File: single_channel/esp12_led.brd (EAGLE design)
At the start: 100 x 80 mm, 10 parts

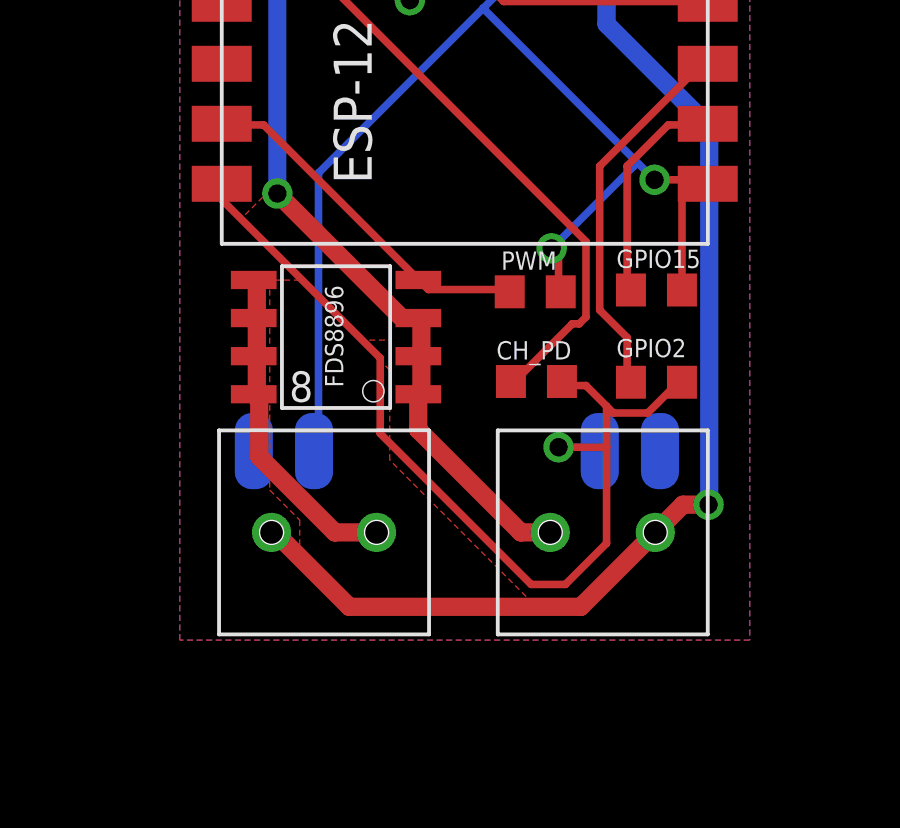
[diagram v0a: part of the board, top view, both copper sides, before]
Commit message: Improved design: Added triple channel (RGB) support, beefed up to ~8.5A per channel.
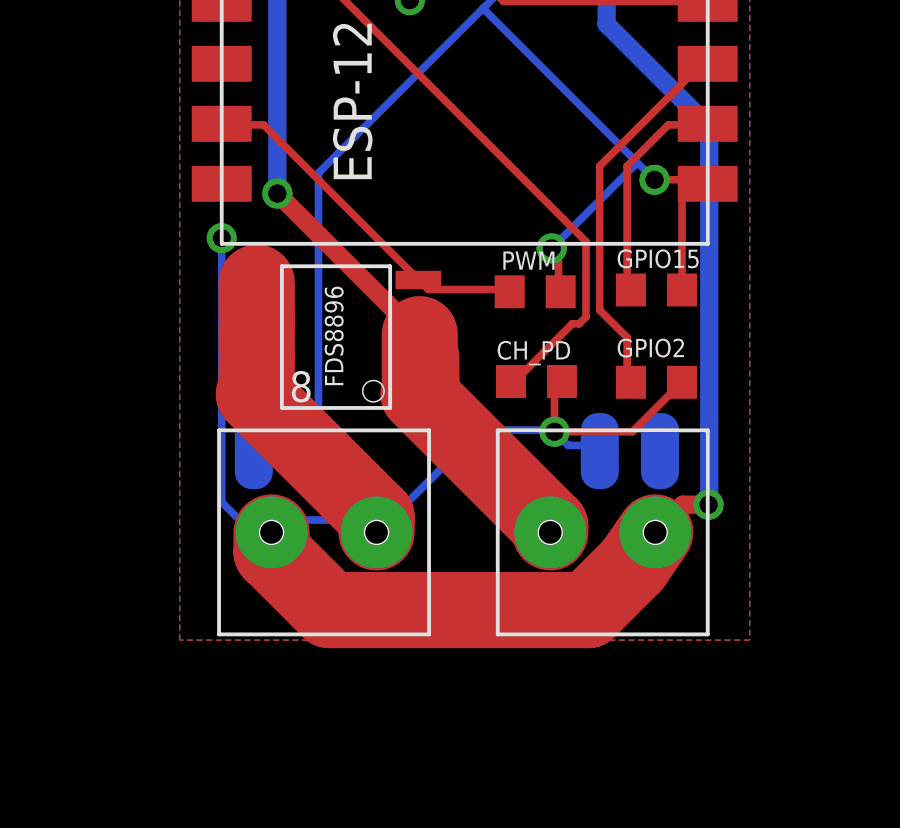
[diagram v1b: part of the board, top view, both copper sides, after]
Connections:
- new net S$3: 12V_IN.1, FDS8896.1, FDS8896.2
- net N$10: no longer 12V_IN.1, FDS8896.1, FDS8896.2
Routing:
- net S$3: track 0.00 -> 10.00 mm
- net N$10: track 26.9 -> 17.4 mm
- net N$1: track 33.2 -> 29.9 mm, vias 1 -> 2
- net N$4: track 11.2 -> 10.4 mm
- net N$12: track 39.4 -> 40.0 mm
- removed copper zone on layer 1, net S$4
- removed copper zone on layer 1, net S$5
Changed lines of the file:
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@@
 <signals>
 <signal name="S$1">
-<polygon width="0.1" layer="1" spacing="0.3048" pour="hatch" isolate="0.254">
+<polygon width="0.1" layer="1" spacing="0.3048" isolate="0.254">
 <vertex x="33" y="53.43"/>
 <vertex x="52" y="53.43"/>
@@
 <vertex x="33" y="23"/>
 </polygon>
-<polygon width="0.1" layer="16" spacing="0.3048" pour="hatch" isolate="0.254">
+<polygon width="0.1" layer="16" spacing="0.3048" isolate="0.254">
 <vertex x="33" y="53.43"/>
 <vertex x="52" y="53.43"/>
@@
 <contactref element="DC_CONVERTER" pad="OUT+(1)"/>
 <contactref element="ESP-12" pad="16"/>
-<wire x1="46.5412" y1="31.4856" x2="45.8554" y2="31.4856" width="0.254" layer="1"/>
-<wire x1="47.4556" y1="30.5712" x2="47.227" y2="30.7998" width="0.254" layer="1"/>
-<wire x1="47.227" y1="30.7998" x2="46.5412" y2="31.4856" width="0.254" layer="1"/>
-<wire x1="48.5986" y1="30.5712" x2="47.4556" y2="30.5712" width="0.254" layer="1"/>
-<wire x1="49.513" y1="31.4856" x2="48.5986" y2="30.5712" width="0.254" layer="1"/>
-<wire x1="45.8554" y1="31.4856" x2="45.74" y2="31.62" width="0.254" layer="1"/>
-<wire x1="49.513" y1="31.4856" x2="49.74" y2="31.595" width="0.254" layer="1"/>
-<wire x1="34.4254" y1="37.6578" x2="34.4254" y2="38.115" width="0.254" layer="1"/>
-<wire x1="39.6832" y1="32.4" x2="34.4254" y2="37.6578" width="0.254" layer="1"/>
-<wire x1="39.6832" y1="29.8854" x2="39.6832" y2="32.4" width="0.254" layer="1"/>
-<wire x1="44.7124" y1="24.8562" x2="39.6832" y2="29.8854" width="0.254" layer="1"/>
-<wire x1="45.8554" y1="24.8562" x2="44.7124" y2="24.8562" width="0.254" layer="1"/>
-<wire x1="47.227" y1="26.2278" x2="45.8554" y2="24.8562" width="0.254" layer="1"/>
-<wire x1="47.227" y1="30.7998" x2="47.227" y2="29.4282" width="0.254" layer="1"/>
-<wire x1="47.227" y1="29.4282" x2="47.227" y2="26.2278" width="0.254" layer="1"/>
-<wire x1="34.4254" y1="38.115" x2="34.4" y2="38.21" width="0.254" layer="1"/>
-<wire x1="45.6268" y1="29.4282" x2="46.9984" y2="29.4282" width="0.254" layer="16"/>
-<wire x1="47.227" y1="29.4282" x2="45.6268" y2="29.4282" width="0.254" layer="1"/>
-<wire x1="46.9984" y1="29.4282" x2="47.0016" y2="29.3" width="0.254" layer="16"/>
-<via x="45.6268" y="29.4282" extent="1-16" drill="0.6096"/>
+<wire x1="45.9486" y1="29.4894" x2="46.863" y2="29.4894" width="0.254" layer="16"/>
+<wire x1="45.4914" y1="29.9466" x2="45.9486" y2="29.4894" width="0.254" layer="16"/>
+<wire x1="45.4914" y1="31.3182" x2="45.4914" y2="29.9466" width="0.254" layer="1"/>
+<wire x1="45.72" y1="31.5468" x2="45.4914" y2="31.3182" width="0.254" layer="1"/>
+<wire x1="46.863" y1="29.4894" x2="47.0016" y2="29.3" width="0.254" layer="16"/>
+<wire x1="45.72" y1="31.5468" x2="45.74" y2="31.62" width="0.254" layer="1"/>
+<via x="45.4914" y="29.9466" extent="1-16" drill="0.6096"/>
+<via x="34.4" y="36.4" extent="1-16" drill="0.6"/>
+<wire x1="34.4" y1="36.4" x2="34.4" y2="27.6" width="0.254" layer="16"/>
+<wire x1="34.4" y1="27.6" x2="35" y2="27" width="0.254" layer="16"/>
+<wire x1="35" y1="27" x2="40" y2="27" width="0.254" layer="16"/>
+<wire x1="40" y1="27" x2="43" y2="30" width="0.254" layer="16"/>
+<wire x1="43" y1="30" x2="45.438" y2="30" width="0.254" layer="16"/>
+<wire x1="45.438" y1="30" x2="45.4914" y2="29.9466" width="0.254" layer="16"/>
+<wire x1="49.74" y1="31.595" x2="48.0916" y2="29.9466" width="0.254" layer="1"/>
+<wire x1="48.0916" y1="29.9466" x2="45.4914" y2="29.9466" width="0.254" layer="1"/>
+<wire x1="34.4" y1="36.4" x2="34.4" y2="38.21" width="0" layer="19" extent="1-1"/>
 </signal>
 <signal name="N$2">
@@
 <contactref element="FDS8896" pad="8"/>
 <contactref element="LED" pad="2"/>
-<wire x1="35.5684" y1="32.4" x2="35.5684" y2="31.257" width="0.6096" layer="1"/>
+<wire x1="35.5684" y1="32.4" x2="35.5684" y2="31.257" width="2.54" layer="1"/>
 <wire x1="35.5684" y1="31.257" x2="35.4668" y2="31.195" width="0.254" layer="1"/>
 <wire x1="35.5684" y1="32.4" x2="35.4668" y2="32.465" width="0.254" layer="1"/>
-<wire x1="35.5684" y1="32.6286" x2="35.5684" y2="33.543" width="0.6096" layer="1"/>
+<wire x1="35.5684" y1="32.6286" x2="35.5684" y2="33.543" width="2.54" layer="1"/>
 <wire x1="35.5684" y1="33.543" x2="35.4668" y2="33.735" width="0.254" layer="1"/>
 <wire x1="35.5684" y1="32.6286" x2="35.4668" y2="32.465" width="0.254" layer="1"/>
-<wire x1="35.5684" y1="33.7716" x2="35.5684" y2="34.9146" width="0.6096" layer="1"/>
+<wire x1="35.5684" y1="33.7716" x2="35.5684" y2="34.9146" width="2.54" layer="1"/>
 <wire x1="35.5684" y1="34.9146" x2="35.4668" y2="35.005" width="0.254" layer="1"/>
 <wire x1="35.5684" y1="33.7716" x2="35.4668" y2="33.735" width="0.254" layer="1"/>
-<wire x1="39.56" y1="26.59" x2="38.17" y2="26.59" width="0.6096" layer="1"/>
-<wire x1="38.17" y1="26.59" x2="35.65" y2="29.11" width="0.6096" layer="1"/>
-<wire x1="35.65" y1="29.11" x2="35.65" y2="31.0118" width="0.6096" layer="1"/>
-<wire x1="35.65" y1="31.0118" x2="35.4668" y2="31.195" width="0.6096" layer="1"/>
+<wire x1="39.56" y1="26.59" x2="39.56" y2="27.1018" width="2.54" layer="1"/>
+<wire x1="39.56" y1="27.1018" x2="35.4668" y2="31.195" width="2.54" layer="1"/>
+</signal>
+<signal name="S$3">
+<contactref element="FDS8896" pad="2"/>
+<wire x1="41.0548" y1="32.6286" x2="40.9532" y2="32.465" width="0.254" layer="1"/>
+<contactref element="FDS8896" pad="1"/>
+<wire x1="41.0548" y1="32.4" x2="40.9532" y2="32.465" width="0.254" layer="1"/>
+<wire x1="41.0548" y1="32.4" x2="41.0548" y2="31.257" width="2.54" layer="1"/>
+<wire x1="41.0548" y1="31.257" x2="40.9532" y2="31.195" width="0.254" layer="1"/>
+<contactref element="12V_IN" pad="1"/>
+<wire x1="41.0548" y1="31.257" x2="41" y2="31.257" width="2.54" layer="1"/>
+<wire x1="41" y1="31.257" x2="41" y2="33.2" width="2.54" layer="1"/>
+<wire x1="45.35" y1="26.59" x2="45.35" y2="26.7982" width="2.54" layer="1"/>
+<wire x1="45.35" y1="26.7982" x2="40.9532" y2="31.195" width="2.54" layer="1"/>
 </signal>
 <signal name="N$10">
-<contactref element="12V_IN" pad="1"/>
-<contactref element="FDS8896" pad="1"/>
-<contactref element="FDS8896" pad="2"/>
 <contactref element="FDS8896" pad="3"/>
 <contactref element="DC_CONVERTER" pad="IN-(1)"/>
-<wire x1="41.0548" y1="32.4" x2="41.0548" y2="31.257" width="0.6096" layer="1"/>
-<wire x1="41.0548" y1="31.257" x2="40.9532" y2="31.195" width="0.254" layer="1"/>
-<wire x1="41.0548" y1="32.4" x2="40.9532" y2="32.465" width="0.254" layer="1"/>
-<wire x1="41.0548" y1="32.6286" x2="41.0548" y2="33.543" width="0.6096" layer="1"/>
 <wire x1="41.0548" y1="33.543" x2="40.9532" y2="33.735" width="0.254" layer="1"/>
-<wire x1="41.0548" y1="32.6286" x2="40.9532" y2="32.465" width="0.254" layer="1"/>
 <wire x1="40.369" y1="33.7716" x2="40.8262" y2="33.7716" width="0.254" layer="1"/>
 <wire x1="36.2542" y1="37.8864" x2="40.369" y2="33.7716" width="0.6096" layer="1"/>
@@
 <wire x1="35.5684" y1="48.1734" x2="35.47" y2="48.35" width="0.254" layer="16"/>
 <via x="36.2542" y="37.8864" extent="1-16" drill="0.6096"/>
-<wire x1="45.35" y1="26.59" x2="44.37" y2="26.59" width="0.6096" layer="1"/>
-<wire x1="44.37" y1="26.59" x2="40.95" y2="30.01" width="0.6096" layer="1"/>
-<wire x1="40.95" y1="30.01" x2="40.95" y2="31.1918" width="0.6096" layer="1"/>
-<wire x1="40.95" y1="31.1918" x2="40.9532" y2="31.195" width="0.6096" layer="1"/>
 </signal>
 <signal name="N$12">
@@
 <contactref element="DC_CONVERTER" pad="IN+(1)"/>
 <contactref element="12V_IN" pad="2"/>
-<wire x1="36.06" y1="26.59" x2="36.17" y2="26.59" width="0.6096" layer="1"/>
-<wire x1="36.17" y1="26.59" x2="38.65" y2="24.11" width="0.6096" layer="1"/>
-<wire x1="38.65" y1="24.11" x2="46.37" y2="24.11" width="0.6096" layer="1"/>
-<wire x1="46.37" y1="24.11" x2="48.85" y2="26.59" width="0.6096" layer="1"/>
 <wire x1="47.227" y1="48.1734" x2="47.0016" y2="48.35" width="0.254" layer="16"/>
 <via x="50.6274" y="27.5138" extent="1-16" drill="0.6096"/>
@@
 <wire x1="50.65" y1="40.11" x2="50.65" y2="27.7364" width="0.6096" layer="16"/>
 <wire x1="50.65" y1="27.7364" x2="50.6274" y2="27.5138" width="0.6096" layer="16"/>
+<wire x1="36.06" y1="26.59" x2="36.06" y2="25.94" width="2.54" layer="1"/>
+<wire x1="36.06" y1="25.94" x2="38" y2="24" width="2.54" layer="1"/>
+<wire x1="38" y1="24" x2="46.6" y2="24" width="2.54" layer="1"/>
+<wire x1="46.6" y1="24" x2="48.1" y2="25.5" width="2.54" layer="1"/>
+<wire x1="48.1" y1="25.5" x2="48.85" y2="26.59" width="2.54" layer="1"/>
 </signal>
 <signal name="N$5">
@@
 <wire x1="40.8262" y1="35.1432" x2="40.9532" y2="35.005" width="0.254" layer="1"/>
 </signal>
-<signal name="S$5">
-<polygon width="0.254" layer="1" isolate="0.254">
-<vertex x="37" y="35"/>
-<vertex x="36" y="35"/>
-<vertex x="36" y="28"/>
-<vertex x="37" y="27"/>
-<vertex x="37" y="26"/>
-<vertex x="38" y="25"/>
-<vertex x="39" y="24"/>
-<vertex x="45" y="24"/>
-<vertex x="40" y="29"/>
-<vertex x="40" y="32"/>
-</polygon>
-</signal>
-<signal name="S$4">
-<polygon width="0.254" layer="1" isolate="0.254">
-<vertex x="40" y="33"/>
-<vertex x="40" y="34"/>
-<vertex x="36" y="38"/>
-<vertex x="35" y="37"/>
-<vertex x="39" y="33"/>
-</polygon>
-</signal>
 </signals>
-<errors>
-</errors>
 </board>
 </drawing>
